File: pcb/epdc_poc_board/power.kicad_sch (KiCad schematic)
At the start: 34 parts, among them J202 USB_C_Receptacle_USB2.0, U104 XC6206PxxxMR, U203 XC6206PxxxMR, U204 SY8008, U205 SY8008, U206 SY8008

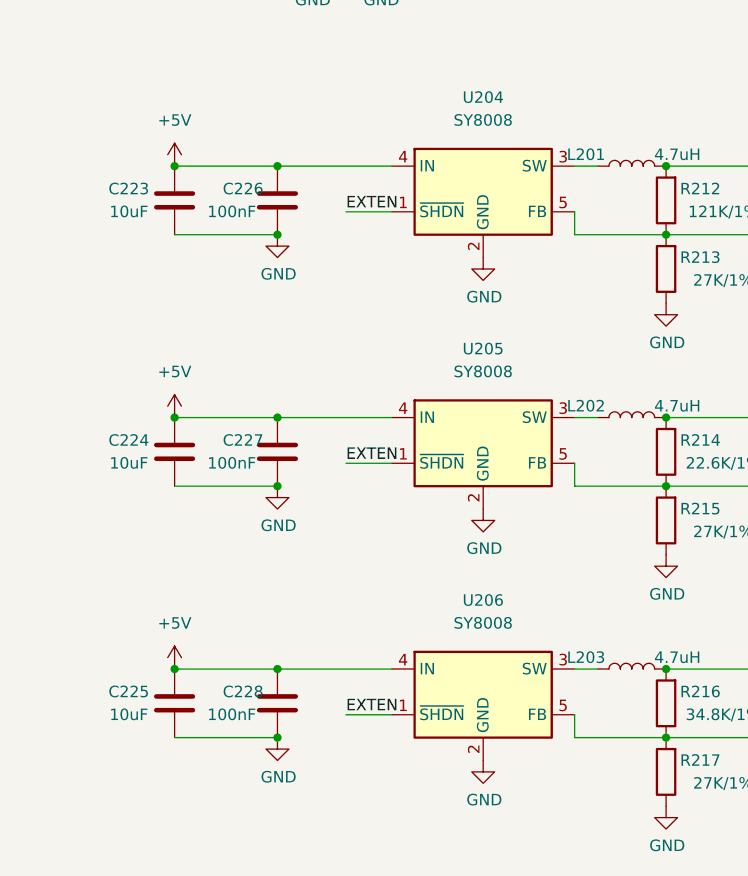
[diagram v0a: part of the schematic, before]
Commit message: - wip epdc poc board, going to remove vga input
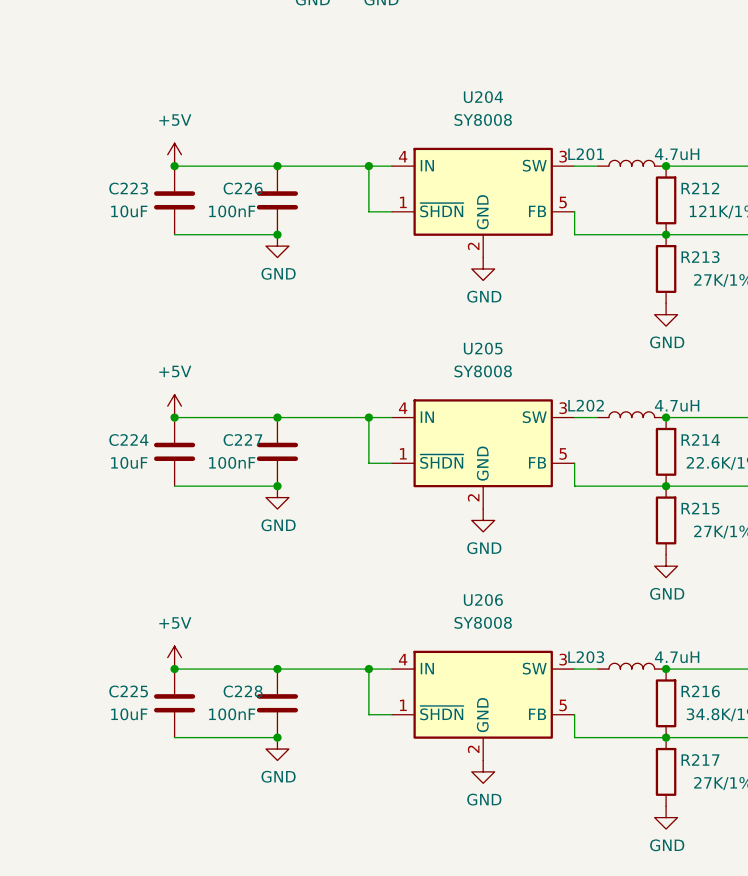
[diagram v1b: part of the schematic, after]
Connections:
- net EXTEN is gone; now on net +5V: U204.1 (~{SHDN}), U205.1 (~{SHDN}), U206.1 (~{SHDN})
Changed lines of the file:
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@@
   (junction (at 55.88 173.99) (diameter 0.9144) (color 0 0 0 0))
   (junction (at 55.88 181.61) (diameter 0.9144) (color 0 0 0 0))
+  (junction (at 66.04 118.11) (diameter 0) (color 0 0 0 0))
+  (junction (at 66.04 146.05) (diameter 0) (color 0 0 0 0))
+  (junction (at 66.04 173.99) (diameter 0) (color 0 0 0 0))
   (junction (at 97.79 36.83) (diameter 0.9144) (color 0 0 0 0))
   (junction (at 97.79 64.77) (diameter 0) (color 0 0 0 0))
@@
     (stroke (width 0) (type solid) (color 0 0 0 0))
   )
-  (wire (pts (xy 55.88 118.11) (xy 68.58 118.11))
+  (wire (pts (xy 55.88 118.11) (xy 66.04 118.11))
     (stroke (width 0) (type solid) (color 0 0 0 0))
   )
-  (wire (pts (xy 55.88 146.05) (xy 68.58 146.05))
+  (wire (pts (xy 55.88 146.05) (xy 66.04 146.05))
     (stroke (width 0) (type solid) (color 0 0 0 0))
   )
-  (wire (pts (xy 55.88 173.99) (xy 68.58 173.99))
+  (wire (pts (xy 55.88 173.99) (xy 66.04 173.99))
     (stroke (width 0) (type solid) (color 0 0 0 0))
   )
-  (wire (pts (xy 63.5 123.19) (xy 68.58 123.19))
+  (wire (pts (xy 66.04 118.11) (xy 66.04 123.19))
+    (stroke (width 0) (type default) (color 0 0 0 0))
+  )
+  (wire (pts (xy 66.04 118.11) (xy 68.58 118.11))
     (stroke (width 0) (type solid) (color 0 0 0 0))
   )
-  (wire (pts (xy 63.5 151.13) (xy 68.58 151.13))
+  (wire (pts (xy 66.04 146.05) (xy 68.58 146.05))
     (stroke (width 0) (type solid) (color 0 0 0 0))
   )
-  (wire (pts (xy 63.5 179.07) (xy 68.58 179.07))
+  (wire (pts (xy 66.04 151.13) (xy 66.04 146.05))
+    (stroke (width 0) (type default) (color 0 0 0 0))
+  )
+  (wire (pts (xy 66.04 173.99) (xy 68.58 173.99))
     (stroke (width 0) (type solid) (color 0 0 0 0))
+  )
+  (wire (pts (xy 66.04 179.07) (xy 66.04 173.99))
+    (stroke (width 0) (type default) (color 0 0 0 0))
+  )
+  (wire (pts (xy 68.58 123.19) (xy 66.04 123.19))
+    (stroke (width 0) (type default) (color 0 0 0 0))
+  )
+  (wire (pts (xy 68.58 151.13) (xy 66.04 151.13))
+    (stroke (width 0) (type default) (color 0 0 0 0))
+  )
+  (wire (pts (xy 68.58 179.07) (xy 66.04 179.07))
+    (stroke (width 0) (type default) (color 0 0 0 0))
   )
   (wire (pts (xy 82.55 36.83) (xy 97.79 36.83))
@@
     (stroke (width 0) (type default) (color 0 0 0 0))
   )
-  (label "EXTEN" (at 63.5 123.19 0)
-    (effects (font (size 1.27 1.27)) (justify left bottom))
-  )
-  (label "EXTEN" (at 63.5 151.13 0)
-    (effects (font (size 1.27 1.27)) (justify left bottom))
-  )
-  (label "EXTEN" (at 63.5 179.07 0)
-    (effects (font (size 1.27 1.27)) (justify left bottom))
-  )
   (symbol (lib_id "power:+5V") (at 44.45 118.11 0) (unit 1)

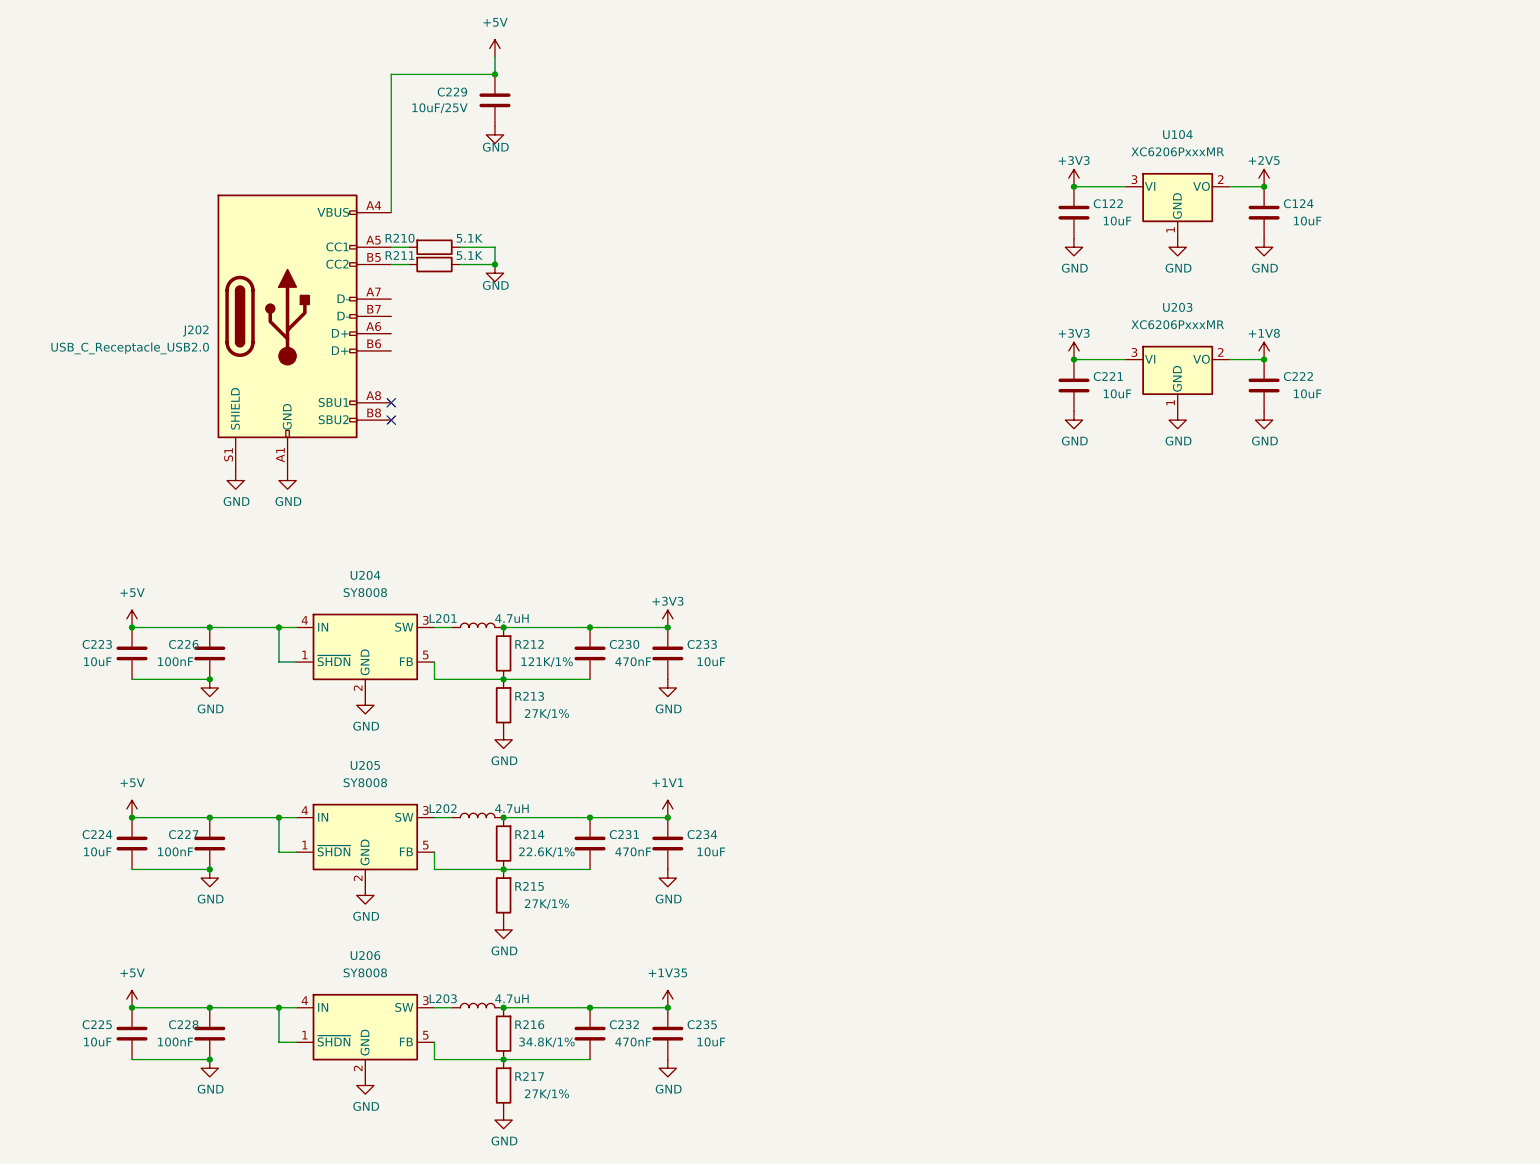
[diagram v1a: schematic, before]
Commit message: pcb: switch to s6 for epdc board
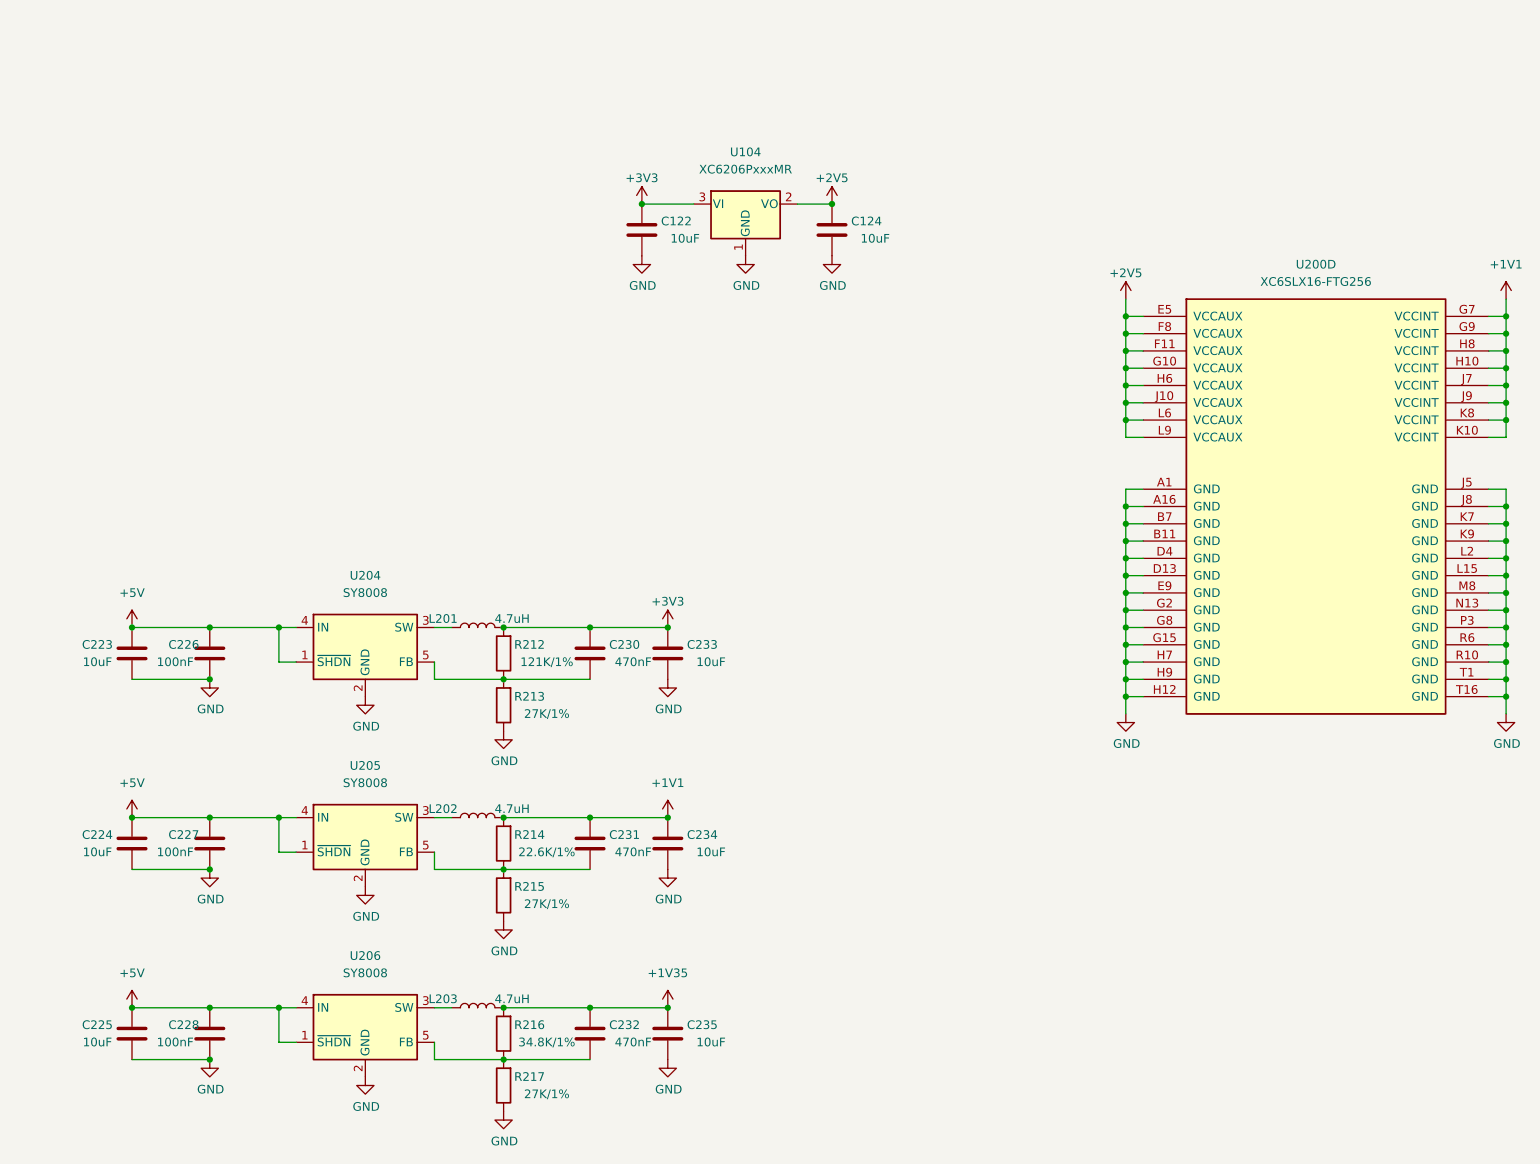
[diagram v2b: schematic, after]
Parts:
- removed C221, C222: 10uF, Capacitor_SMD:C_0603_1608Metric, symbol Device:C
- removed C229: 10uF/25V, Capacitor_SMD:C_0805_2012Metric, symbol Device:C
- removed J202: USB_C_Receptacle_USB2.0, Connector_USB:USB_C_Receptacle_HRO_TYPE-C-31-M-12, symbol Connector:USB_C_Receptacle_USB2.0
- removed R210, R211: 5.1K, Resistor_SMD:R_0402_1005Metric, symbol Device:R
- removed U203: XC6206PxxxMR, Package_TO_SOT_SMD:SOT-23, symbol Regulator_Linear:XC6206PxxxMR
- added U200: XC6SLX16-FTG256, Package_BGA:BGA-256_14.0x14.0mm_Layout16x16_P0.8mm_Ball0.45mm_Pad0.32mm_NSMD, symbol FPGA_Xilinx_Spartan6:XC6SLX16-FTG256
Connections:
- net +1V1: now also U200.G7 (VCCINT), U200.G9 (VCCINT), U200.H10 (VCCINT), U200.H8 (VCCINT), U200.J7 (VCCINT), U200.J9 (VCCINT), U200.K10 (VCCINT), U200.K8 (VCCINT)
- net +2V5: now also U200.E5 (VCCAUX), U200.F11 (VCCAUX), U200.F8 (VCCAUX), U200.G10 (VCCAUX), U200.H6 (VCCAUX), U200.J10 (VCCAUX), U200.L6 (VCCAUX), U200.L9 (VCCAUX)
- net GND: now also U200.A1 (GND), U200.A16 (GND), U200.B11 (GND), U200.B7 (GND), U200.D13 (GND), U200.D4 (GND), U200.E9 (GND), U200.G15 (GND), U200.G2 (GND), U200.G8 (GND), U200.H12 (GND), U200.H7 (GND), U200.H9 (GND), U200.J5 (GND), U200.J8 (GND), U200.K7 (GND), U200.K9 (GND), U200.L15 (GND), U200.L2 (GND), U200.M8 (GND), U200.N13 (GND), U200.P3 (GND), U200.R10 (GND), U200.R6 (GND), U200.T1 (GND), U200.T16 (GND)
- no-connect marks 2 -> 0
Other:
- moved on the sheet: C122, C124, U104

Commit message: pcb: mb r0.1, caster r0.1 freeze
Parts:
- C122, C124, C233, C234, C235: LCSC (none) -> C105490; Ref.Price (none) -> 0.0165
- C223, C224, C225: footprint Capacitor_SMD:C_0805_2012Metric -> Capacitor_SMD:C_0603_1608Metric; LCSC (none) -> C105490; Ref.Price (none) -> 0.0165
- C226, C227, C228: LCSC (none) -> C56392; Ref.Price (none) -> 0.0023
- C230, C231, C232: value 470nF -> 220nF; LCSC (none) -> C880414; Ref.Price (none) -> 0.0036
- L201, L202, L203: LCSC (none) -> C340379; Ref.Price (none) -> 0.0643
- R212: LCSC (none) -> C112303; Ref.Price (none) -> 0.001
- R213, R215, R217: LCSC (none) -> C138022; Ref.Price (none) -> 0.0029
- R214: LCSC (none) -> C477674; Ref.Price (none) -> 0.0006
- R216: LCSC (none) -> C327350; Ref.Price (none) -> 0.001
- U104: value XC6206PxxxMR -> XC6206P252MR; LCSC (none) -> C15906; Ref.Price (none) -> 0.1086
- U200: LCSC (none) -> C39313; Ref.Price (none) -> 7.4837
- U204, U205, U206: LCSC (none) -> C82161; Ref.Price (none) -> 0.1632
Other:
- company: (none) -> Copyright 2021 Modos / Engineer: Wenting Zhang
- title: (none) -> Caster EPDC
